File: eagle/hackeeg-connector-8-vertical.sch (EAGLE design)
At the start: 19 parts

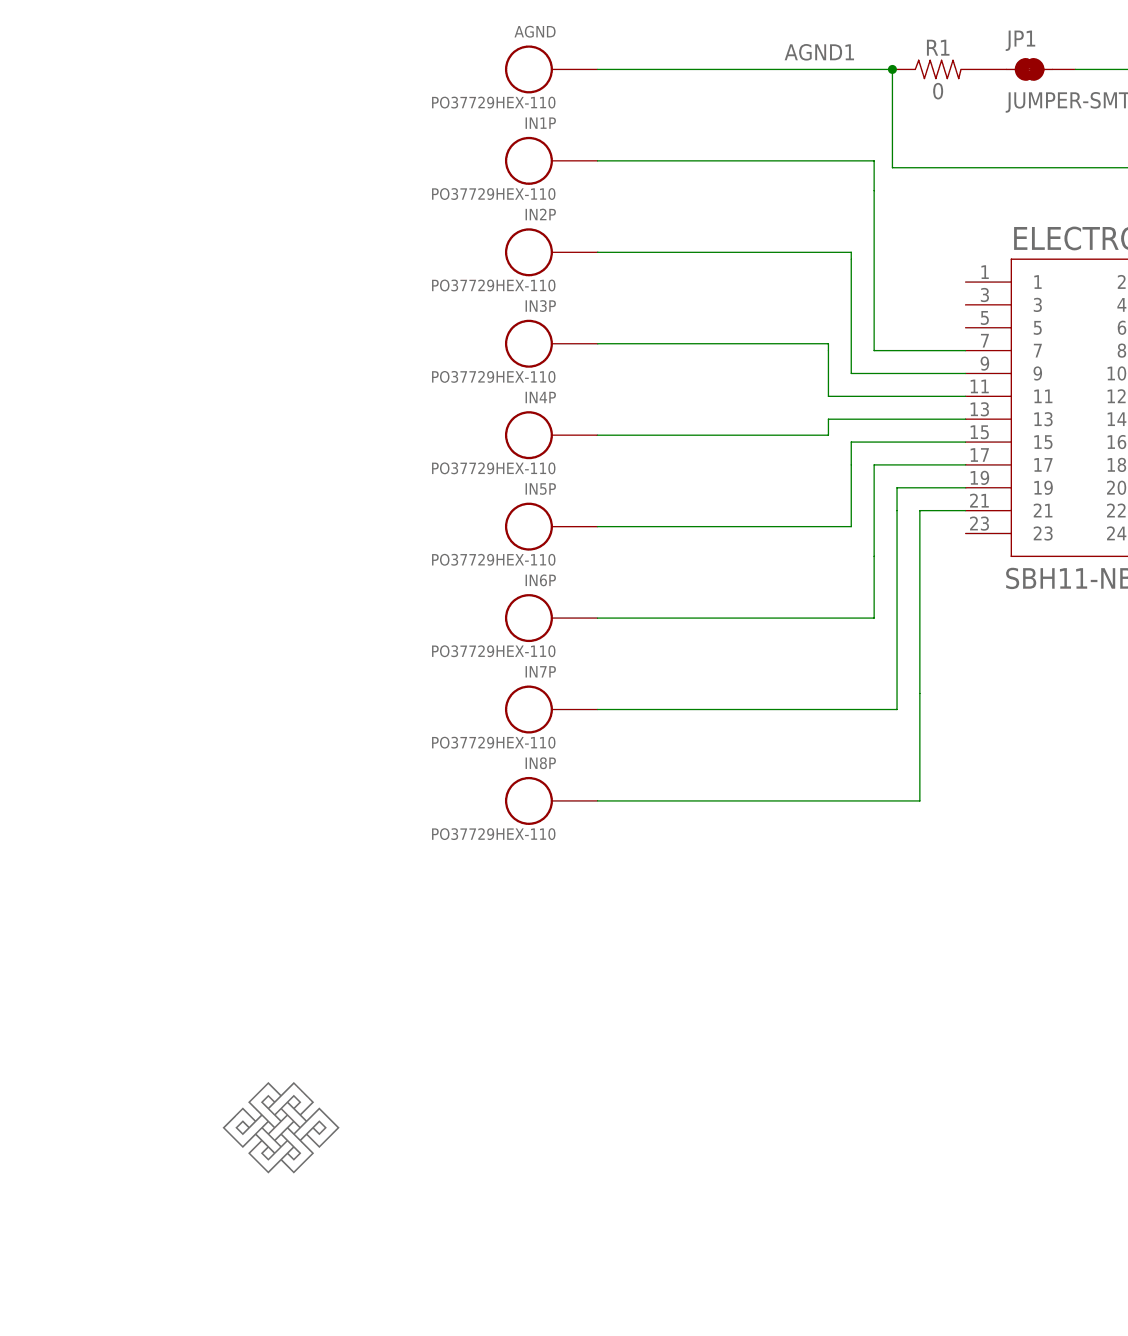
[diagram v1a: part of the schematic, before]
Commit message: add 2-pin JST connector for REF_ELEC multiboard
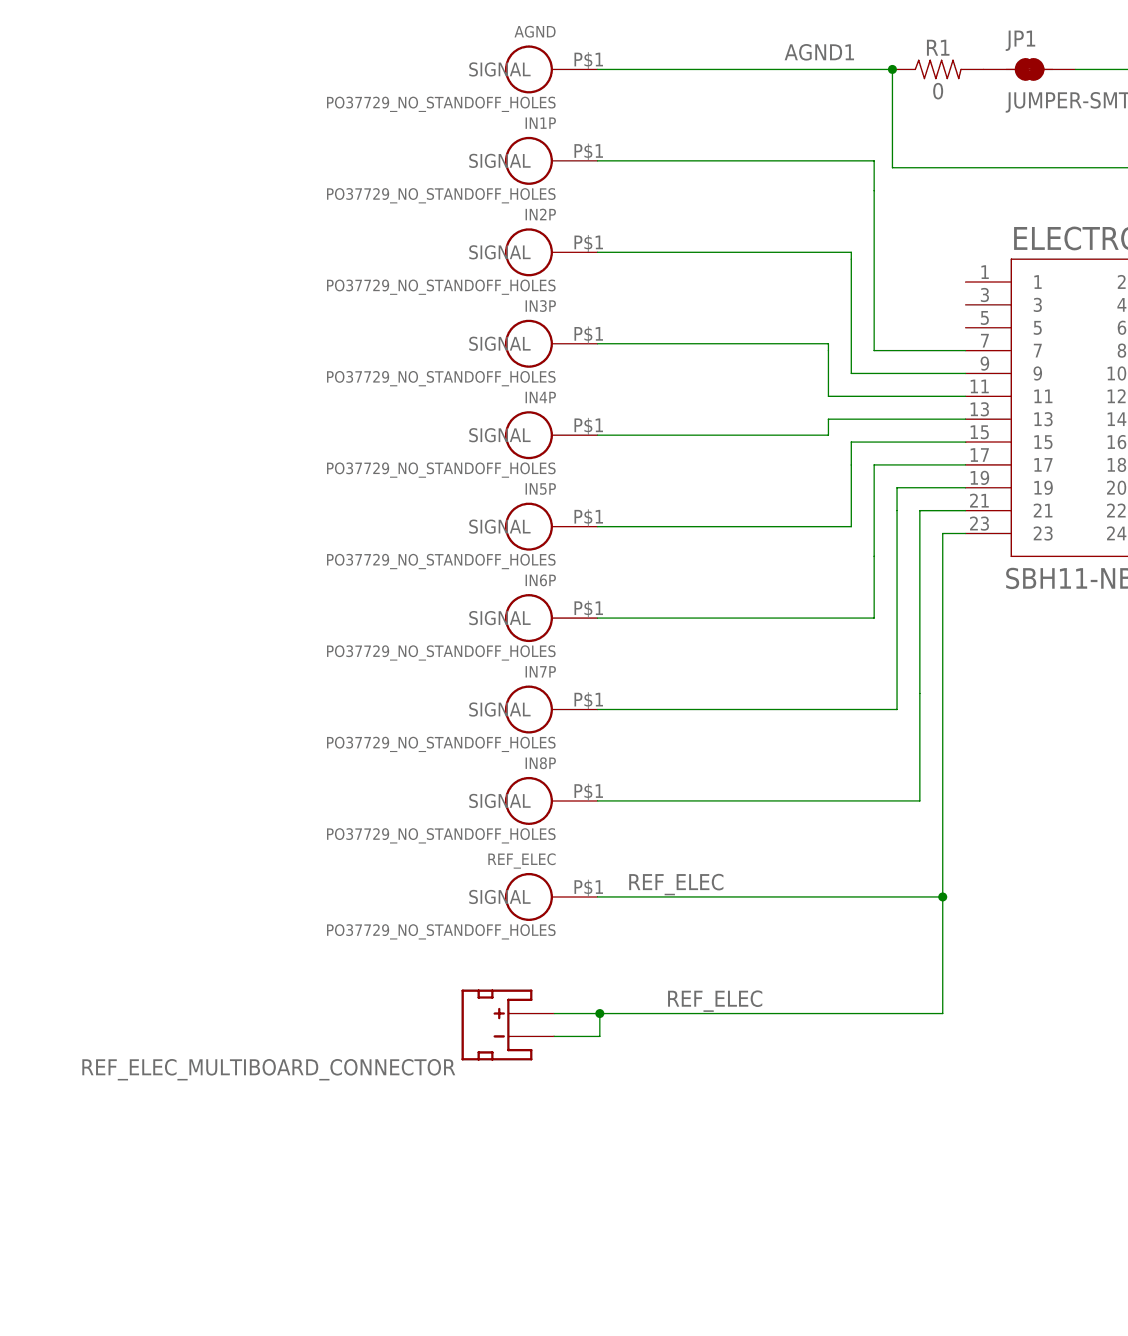
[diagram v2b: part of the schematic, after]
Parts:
- removed U$1: ENDLESSKNOTENDLESSKNOT-MEDIUM, endless-knot:ENDLESSKNOTENDLESSKNOT-MEDIUM
- added REF_ELEC: PO37729_NO_STANDOFF_HOLES, hackeeg-connectors:PO37729_NO_STANDOFF_HOLES
- added REF_ELEC_MULTIBOARD_CONNECTOR: (no value), SparkFun-Connectors:JST_2MM_MALE
- AGND, IN1P, IN2P, IN3P, IN4P, IN5P, IN6P, IN7P, IN8P: value PO37729HEX-110 -> PO37729_NO_STANDOFF_HOLES; device po-37729:PO37729HEX-110 -> hackeeg-connectors:PO37729_NO_STANDOFF_HOLES
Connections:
- new net REF_ELEC: ELECTRODE-CONNECTOR.23, REF_ELEC.SIGNAL, REF_ELEC_MULTIBOARD_CONNECTOR.+, REF_ELEC_MULTIBOARD_CONNECTOR.-
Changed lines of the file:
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@@
 <?xml version="1.0" encoding="utf-8"?>
 <!DOCTYPE eagle SYSTEM "eagle.dtd">
-<eagle version="9.4.0">
+<eagle version="9.5.2">
 <drawing>
 <settings>
@@
 <layer number="230" name="230bmp" color="7" fill="1" visible="yes" active="yes"/>
 <layer number="231" name="231bmp" color="7" fill="1" visible="yes" active="yes"/>
+<layer number="232" name="Eagle3D_PG2" color="7" fill="1" visible="yes" active="yes"/>
+<layer number="233" name="Eagle3D_PG3" color="7" fill="1" visible="yes" active="yes"/>
 <layer number="248" name="Housing" color="7" fill="1" visible="yes" active="yes"/>
 <layer number="249" name="Edge" color="7" fill="1" visible="yes" active="yes"/>
@@
 </classes>
 <parts>
-<part name="IN1P" library="po-37729" deviceset="PO37729" device="HEX-110" value="PO37729HEX-110"/>
+<part name="IN1P" library="hackeeg-connectors" deviceset="PO37729" device="_NO_STANDOFF_HOLES" value="PO37729_NO_STANDOFF_HOLES"/>
 <part name="ELECTRODE-CONNECTOR" library="SBH11-NBPC-D12-SM-BK" deviceset="SBH11-NBPC-D12-SM-BK" device=""/>
-<part name="IN2P" library="po-37729" deviceset="PO37729" device="HEX-110" value="PO37729HEX-110"/>
-<part name="IN3P" library="po-37729" deviceset="PO37729" device="HEX-110" value="PO37729HEX-110"/>
-<part name="IN4P" library="po-37729" deviceset="PO37729" device="HEX-110" value="PO37729HEX-110"/>
-<part name="IN5P" library="po-37729" deviceset="PO37729" device="HEX-110" value="PO37729HEX-110"/>
-<part name="IN6P" library="po-37729" deviceset="PO37729" device="HEX-110" value="PO37729HEX-110"/>
-<part name="IN7P" library="po-37729" deviceset="PO37729" device="HEX-110" value="PO37729HEX-110"/>
-<part name="AGND" library="po-37729" deviceset="PO37729" device="HEX-110" value="PO37729HEX-110"/>
-<part name="IN8P" library="po-37729" deviceset="PO37729" device="HEX-110"/>
-<part name="U$1" library="endless-knot" deviceset="ENDLESSKNOT" device="ENDLESSKNOT-MEDIUM"/>
+<part name="IN2P" library="hackeeg-connectors" deviceset="PO37729" device="_NO_STANDOFF_HOLES" value="PO37729_NO_STANDOFF_HOLES"/>
+<part name="IN3P" library="hackeeg-connectors" deviceset="PO37729" device="_NO_STANDOFF_HOLES" value="PO37729_NO_STANDOFF_HOLES"/>
+<part name="IN4P" library="hackeeg-connectors" deviceset="PO37729" device="_NO_STANDOFF_HOLES" value="PO37729_NO_STANDOFF_HOLES"/>
+<part name="IN5P" library="hackeeg-connectors" deviceset="PO37729" device="_NO_STANDOFF_HOLES" value="PO37729_NO_STANDOFF_HOLES"/>
+<part name="IN6P" library="hackeeg-connectors" deviceset="PO37729" device="_NO_STANDOFF_HOLES" value="PO37729_NO_STANDOFF_HOLES"/>
+<part name="IN7P" library="hackeeg-connectors" deviceset="PO37729" device="_NO_STANDOFF_HOLES" value="PO37729_NO_STANDOFF_HOLES"/>
+<part name="AGND" library="hackeeg-connectors" deviceset="PO37729" device="_NO_STANDOFF_HOLES" value="PO37729_NO_STANDOFF_HOLES"/>
+<part name="IN8P" library="hackeeg-connectors" deviceset="PO37729" device="_NO_STANDOFF_HOLES"/>
 <part name="FD1" library="SparkFun-Aesthetics" library_urn="urn:adsk.eagle:library:507" deviceset="FIDUCIAL" device="1X2" package3d_urn="urn:adsk.eagle:package:37108/1"/>
 <part name="FD2" library="SparkFun-Aesthetics" library_urn="urn:adsk.eagle:library:507" deviceset="FIDUCIAL" device="1X2" package3d_urn="urn:adsk.eagle:package:37108/1"/>
@@
 <part name="JP1" library="SparkFun-Jumpers" library_urn="urn:adsk.eagle:library:528" deviceset="JUMPER-SMT_2_NC_TRACE" device="_NO-SILK" package3d_urn="urn:adsk.eagle:package:39286/1"/>
 <part name="FRAME1" library="frames" library_urn="urn:adsk.eagle:library:229" deviceset="FRAME_A_L" device=""/>
+<part name="REF_ELEC" library="hackeeg-connectors" deviceset="PO37729" device="_NO_STANDOFF_HOLES"/>
+<part name="REF_ELEC_MULTIBOARD_CONNECTOR" library="SparkFun-Connectors" library_urn="urn:adsk.eagle:library:513" deviceset="JST_2MM_MALE" device="" package3d_urn="urn:adsk.eagle:package:38042/1"/>
 </parts>
 <sheets>
@@
 <attribute name="VALUE" x="233.934" y="105.664" size="1.27" layer="95" rot="MR0"/>
 </instance>
-<instance part="U$1" gate="G$1" x="203.2" y="73.66" smashed="yes"/>
 <instance part="FD1" gate="G$1" x="355.6" y="170.18" smashed="yes"/>
 <instance part="FD2" gate="G$1" x="355.6" y="182.88" smashed="yes"/>
@@
 <attribute name="SHEET" x="424.18" y="36.83" size="2.54" layer="94"/>
 <attribute name="DRAWING_NAME" x="355.6" y="54.61" size="2.54" layer="94"/>
+</instance>
+<instance part="REF_ELEC" gate="G$1" x="238.506" y="99.314" smashed="yes" rot="MR0">
+<attribute name="NAME" x="233.934" y="102.87" size="1.27" layer="95" rot="MR0"/>
+<attribute name="VALUE" x="233.934" y="94.996" size="1.27" layer="95" rot="MR0"/>
+</instance>
+<instance part="REF_ELEC_MULTIBOARD_CONNECTOR" gate="G$1" x="228.6" y="83.82" smashed="yes" rot="R90">
+<attribute name="NAME" x="222.758" y="81.28" size="1.778" layer="95" rot="R180"/>
 </instance>
 </instances>
@@
 </segment>
 </net>
+<net name="REF_ELEC" class="0">
+<segment>
+<pinref part="REF_ELEC_MULTIBOARD_CONNECTOR" gate="G$1" pin="+"/>
+<wire x1="233.68" y1="86.36" x2="238.76" y2="86.36" width="0.1524" layer="91"/>
+<junction x="238.76" y="86.36"/>
+<wire x1="238.76" y1="83.82" x2="238.76" y2="86.36" width="0.1524" layer="91"/>
+<pinref part="REF_ELEC_MULTIBOARD_CONNECTOR" gate="G$1" pin="-"/>
+<wire x1="233.68" y1="83.82" x2="238.76" y2="83.82" width="0.1524" layer="91"/>
+<label x="246.126" y="87.122" size="1.778" layer="95"/>
+<wire x1="276.86" y1="86.36" x2="238.76" y2="86.36" width="0.1524" layer="91"/>
+<wire x1="276.86" y1="99.314" x2="276.86" y2="86.36" width="0.1524" layer="91"/>
+<pinref part="ELECTRODE-CONNECTOR" gate="G$1" pin="23"/>
+<wire x1="279.4" y1="139.7" x2="276.86" y2="139.7" width="0.1524" layer="91"/>
+<wire x1="276.86" y1="139.7" x2="276.86" y2="99.314" width="0.1524" layer="91"/>
+<wire x1="276.86" y1="99.314" x2="238.506" y2="99.314" width="0.1524" layer="91"/>
+<pinref part="REF_ELEC" gate="G$1" pin="SIGNAL"/>
+<label x="241.808" y="100.076" size="1.778" layer="95"/>
+<junction x="276.86" y="99.314"/>
+</segment>
+</net>
 </nets>
 </sheet>
 </sheets>
+<errors>
+</errors>
 </schematic>
 </drawing>
